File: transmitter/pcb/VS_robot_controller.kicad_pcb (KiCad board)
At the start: 2 copper layers, 70.5 x 67 mm, 11 parts

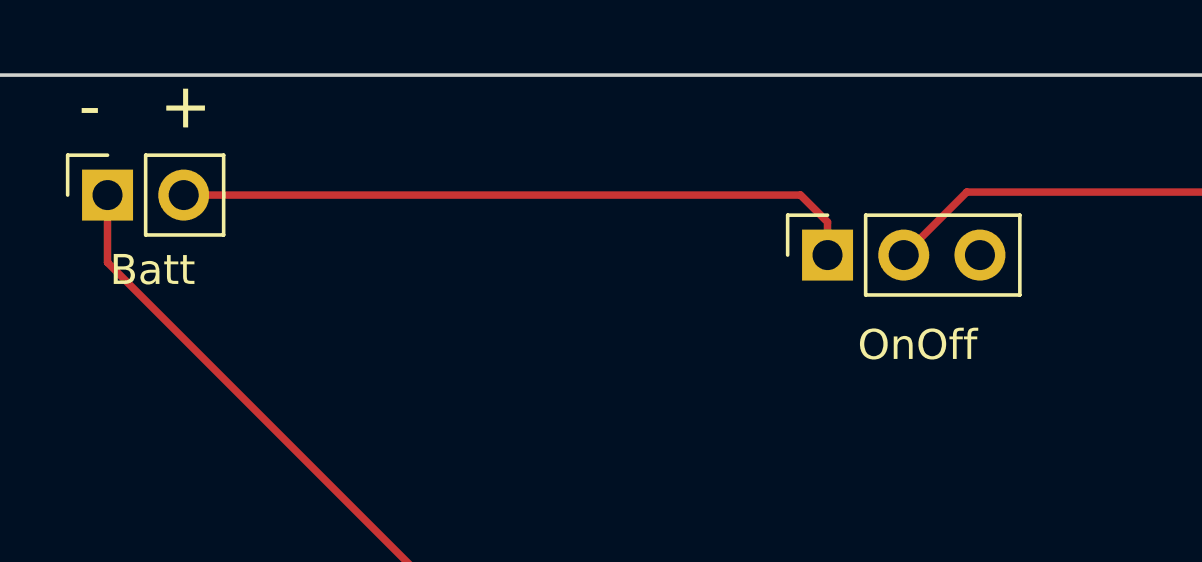
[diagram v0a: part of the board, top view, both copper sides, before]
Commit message: flipped transmitter on/off switch
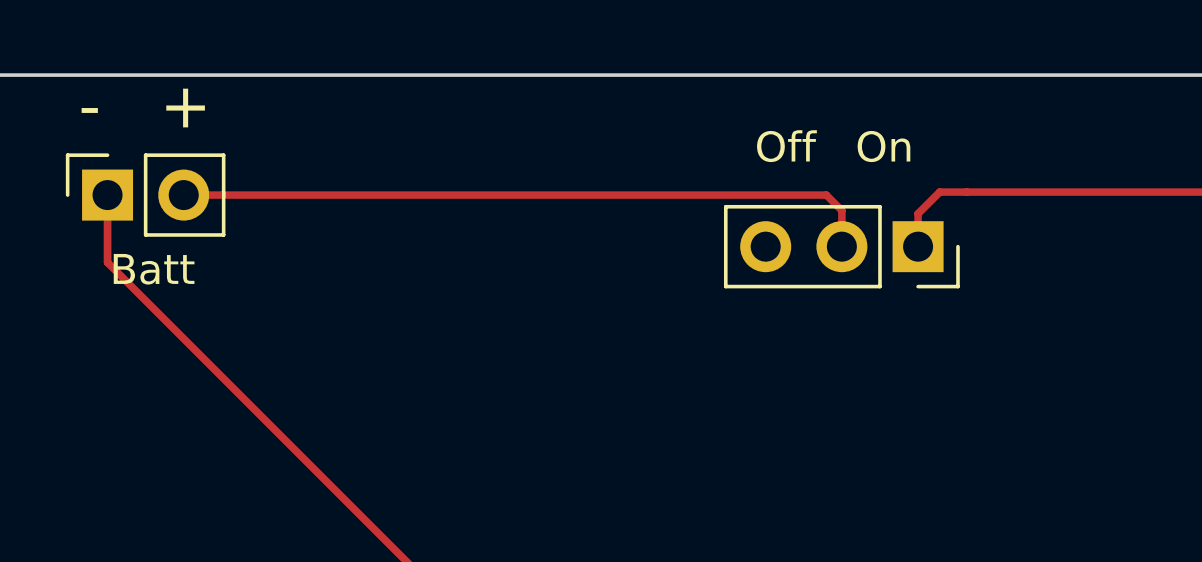
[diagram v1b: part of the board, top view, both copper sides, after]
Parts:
- Off   On: renamed from OnOff
- moved Off   On 3.03 mm to (207.5, 45.7), turned to 270 degrees
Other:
- board text added: "V1.2"
- board text removed: "V1"
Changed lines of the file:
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@@
-(kicad_pcb (version 20171130) (host pcbnew 5.1.2)
+(kicad_pcb (version 20171130) (host pcbnew 5.0.2+dfsg1-1)
   (general
     (thickness 1.6)
     (drawings 12)
-    (tracks 103)
+    (tracks 105)
     (zones 0)
     (modules 11)
@@
     (zone_45_only no)
     (trace_min 0.2)
+    (segment_width 0.2)
+    (edge_width 0.05)
     (via_size 0.8)
     (via_drill 0.4)
@@
     (uvia_min_size 0.2)
     (uvia_min_drill 0.1)
-    (edge_width 0.05)
-    (segment_width 0.2)
     (pcb_text_width 0.3)
     (pcb_text_size 1.5 1.5)
@@
   )
   (module Connector_PinSocket_2.54mm:PinSocket_1x03_P2.54mm_Vertical (layer F.Cu)
-    (at 204.5 46 90)
+    (at 207.518 45.72 270)
     (descr "Through hole straight socket strip, 1x03, 2.54mm pitch, single row (from Kicad 4.0.7), script generated")
     (tags "Through hole socket strip THT 1x03 2.54mm single row")
-    (fp_text reference OnOff (at -3 3 180) (layer F.SilkS)
-      (effects (font (size 1 1) (thickness 0.15)))
-    )
-    (fp_text value sw1 (at 0 7.85 90) (layer F.Fab)
+    (fp_text reference "Off   On" (at -3.302 2.794) (layer F.SilkS)
+      (effects (font (size 1 1) (thickness 0.15)))
+    )
+    (fp_text value sw1 (at 0 7.85 270) (layer F.Fab)
       (effects (font (size 1 1) (thickness 0.15)))
     )
@@
     (fp_line (start 1.75 6.85) (end -1.8 6.85) (layer F.CrtYd) (width 0.05))
     (fp_line (start -1.8 6.85) (end -1.8 -1.8) (layer F.CrtYd) (width 0.05))
-    (fp_text user %R (at 0 2.54) (layer F.Fab)
-      (effects (font (size 1 1) (thickness 0.15)))
-    )
-    (pad 1 thru_hole rect (at 0 0 90) (size 1.7 1.7) (drill 1) (layers *.Cu *.Mask)
+    (fp_text user %R (at 0 2.54 180) (layer F.Fab)
+      (effects (font (size 1 1) (thickness 0.15)))
+    )
+    (pad 1 thru_hole rect (at 0 0 270) (size 1.7 1.7) (drill 1) (layers *.Cu *.Mask)
       (net 3 +12V))
-    (pad 2 thru_hole oval (at 0 2.54 90) (size 1.7 1.7) (drill 1) (layers *.Cu *.Mask)
+    (pad 2 thru_hole oval (at 0 2.54 270) (size 1.7 1.7) (drill 1) (layers *.Cu *.Mask)
       (net 3 +12V))
-    (pad 3 thru_hole oval (at 0 5.08 90) (size 1.7 1.7) (drill 1) (layers *.Cu *.Mask)
+    (pad 3 thru_hole oval (at 0 5.08 270) (size 1.7 1.7) (drill 1) (layers *.Cu *.Mask)
       (net 7 "Net-(OnOff1-Pad3)"))
     (model ${KISYS3DMOD}/Connector_PinSocket_2.54mm.3dshapes/PinSocket_1x03_P2.54mm_Vertical.wrl
@@
     (effects (font (size 1.5 1.5) (thickness 0.3)))
   )
-  (gr_text V1 (at 206.1 55.575) (layer B.SilkS)
+  (gr_text V1.2 (at 206.1 55.575) (layer B.SilkS)
     (effects (font (size 1.5 1.5) (thickness 0.3)) (justify mirror))
   )
@@
   (segment (start 181.23017 94.73017) (end 181.300001 94.800001) (width 0.25) (layer B.Cu) (net 2))
   (segment (start 182.655 68.375) (end 182.30575 68.375) (width 0.25) (layer B.Cu) (net 2))
-  (segment (start 204.5 44.9) (end 204.5 46) (width 0.25) (layer F.Cu) (net 3))
-  (segment (start 203.6 44) (end 204.5 44.9) (width 0.25) (layer F.Cu) (net 3))
-  (segment (start 183.04 44) (end 203.6 44) (width 0.25) (layer F.Cu) (net 3))
   (segment (start 209.14 43.9) (end 228 43.9) (width 0.25) (layer F.Cu) (net 3))
-  (segment (start 207.04 46) (end 209.14 43.9) (width 0.25) (layer F.Cu) (net 3))
+  (segment (start 204.978 44.517919) (end 204.978 45.72) (width 0.25) (layer F.Cu) (net 3))
+  (segment (start 204.460081 44) (end 204.978 44.517919) (width 0.25) (layer F.Cu) (net 3))
+  (segment (start 183.04 44) (end 204.460081 44) (width 0.25) (layer F.Cu) (net 3))
+  (segment (start 208.238 43.9) (end 209.14 43.9) (width 0.25) (layer F.Cu) (net 3))
+  (segment (start 207.518 44.62) (end 208.238 43.9) (width 0.25) (layer F.Cu) (net 3))
+  (segment (start 207.518 45.72) (end 207.518 44.62) (width 0.25) (layer F.Cu) (net 3))
   (segment (start 187.5 98.62) (end 190.12 96) (width 0.25) (layer F.Cu) (net 9))
   (segment (start 187.5 103) (end 187.5 98.62) (width 0.25) (layer F.Cu) (net 9))

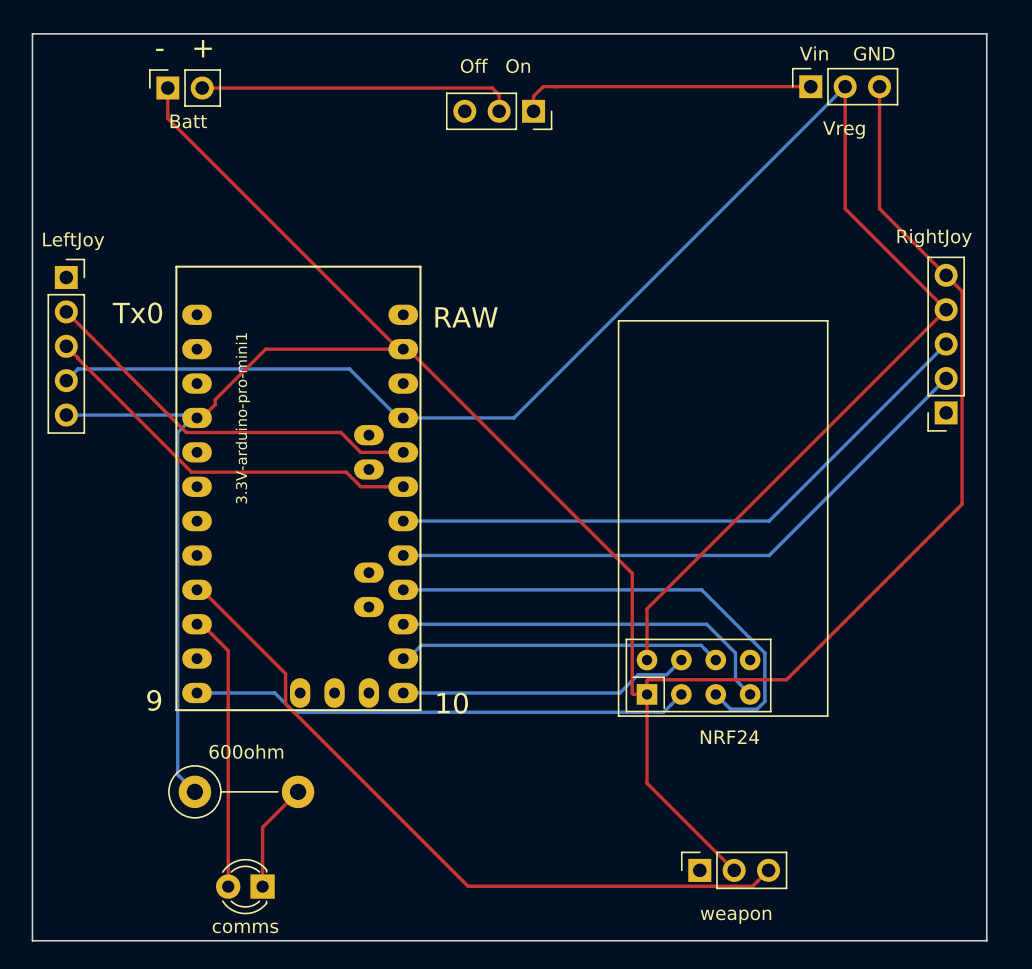
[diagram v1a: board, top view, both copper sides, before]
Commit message: V1.3 of Receiver and 1.2 of Transmitter. These versions were ordered 6/21/22
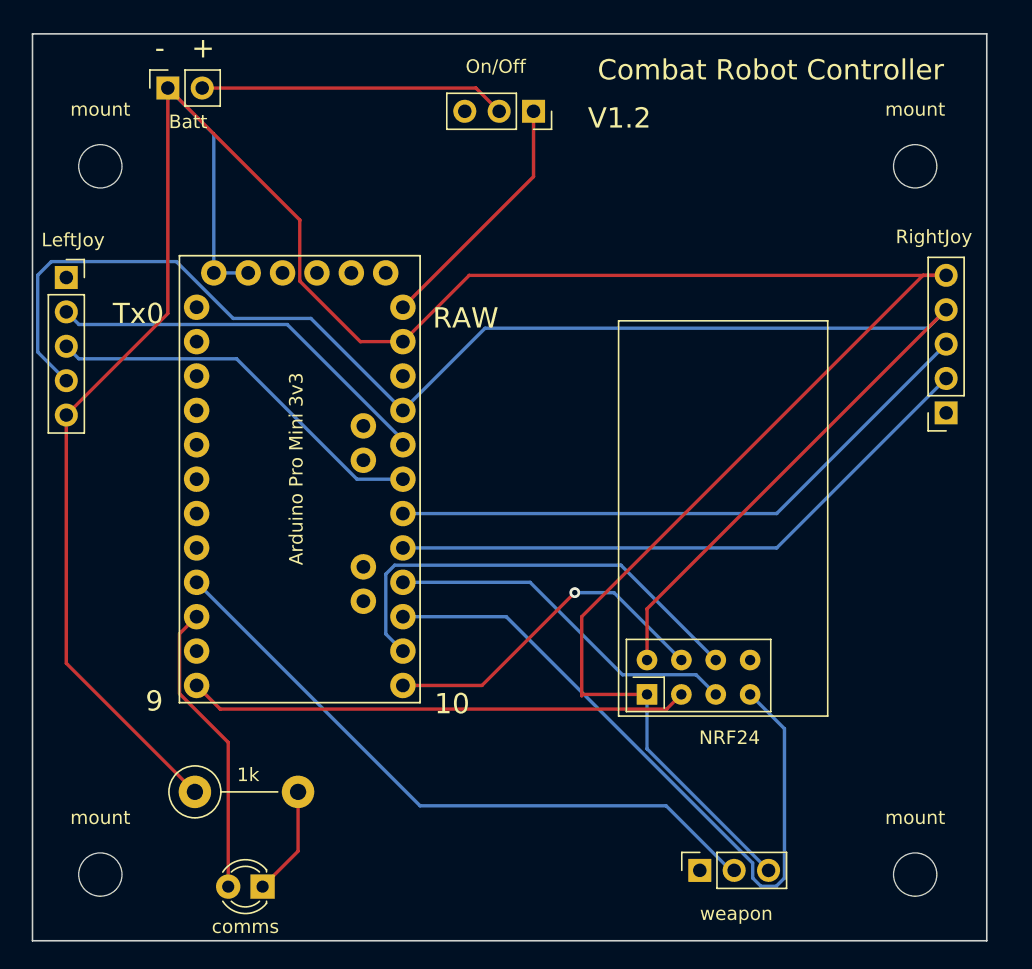
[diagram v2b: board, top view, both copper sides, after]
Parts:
- removed 3.3V-arduino-pro-mini1: arduino-pro-mini, mysensors:pro_mini
- removed the G*** at (206.3, 86.9)
- removed Vreg: j3, Connector_PinSocket_2.54mm:PinSocket_1x03_P2.54mm_Vertical
- added Arduino Pro Mini 3v3: ARDUINO_PRO_MINI, arduino:MODULE_ARDUINO_PRO_MINI, F.Cu at (190.2, 72.9)
- added G***: LOGO, VS_Logo:vs_logo, B.Cu at (204.7, 70.6)
- added mount: MountingHole_3.2mm_M3, MountingHole:MountingHole_3.2mm_M3, F.Cu at (235.7, 49.8)
- added mount: MountingHole_3.2mm_M3, MountingHole:MountingHole_3.2mm_M3, F.Cu at (175.5, 49.8)
- added mount: MountingHole_3.2mm_M3, MountingHole:MountingHole_3.2mm_M3, F.Cu at (175.5, 102.1)
- added mount: MountingHole_3.2mm_M3, MountingHole:MountingHole_3.2mm_M3, F.Cu at (235.7, 102.1)
- On/Off: renamed from Off   On
- renumbered 600ohm to 1k
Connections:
- Batt pad 2: +12V -> +9V
- On/Off pad 1: +12V -> Net-(OnOff1-Pad1)
- On/Off pad 2: +12V -> +9V
- weapon pad 2: GND -> Net-(U2-PadJP7_4)
- weapon pad 3: Net-(3.3V-arduino-pro-mini1-Pad9) -> GND
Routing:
- net Net-(3.3V-arduino-pro-mini1-Pad9): track 53.1 -> 0.00 mm
- net Net-(U2-PadJP7_4): track 0.00 -> 48.5 mm
- net +12V: track 45.2 -> 0.00 mm
- net Net-(U1-Pad7): track 28.9 -> 52.0 mm
- net +9V: track 0.00 -> 22.7 mm
- net Net-(OnOff1-Pad1): track 0.00 -> 18.5 mm
- net GND: track 195.4 -> 211.4 mm
- net Net-(U1-Pad5): track 36.5 -> 26.5 mm
- net Net-(U1-Pad6): track 23.9 -> 33.8 mm
- net +3V3: track 124.1 -> 118.9 mm
- net Net-(U1-Pad4): track 21.6 -> 25.5 mm, vias 0 -> 1
- net Net-(U2-PadJP7_3): track 20.5 -> 22.0 mm
- net Net-(RightJoy1-Pad3): track 46.0 -> 45.3 mm
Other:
- board text removed: "Vin GND"
